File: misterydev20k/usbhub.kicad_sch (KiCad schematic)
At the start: 21 parts, among them J10 USB_A, J7 USB_A, J8 USB_A, J9 USB_A, U7 CH334U, Y3 12MHz

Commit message: More updates in dev20k
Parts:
- removed JP2: CLK, Jumper:SolderJumper-3_P1.3mm_Bridged12_RoundedPad1.0x1.5mm, symbol Jumper:SolderJumper_3_Bridged12
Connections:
- net at U7.3 (XI): now also Y3.1
- net VDD33: no longer names the net of C30.2, C31.2, C32.2, D11.2 (A), U7.13 (VDD33), U7.21 (VDD33)
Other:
- note removed: "2-3 to share OSC with RP2040"
- moved on the sheet: C28, C29, C30, C31, C32, D10, D11, D7, D8, D9, F2, J10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

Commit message: Update board
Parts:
- removed J10, J7, J8, J9: USB_A, Connector_USB:USB_A_Molex_67643_Horizontal, symbol Connector:USB_A
- added J13, J7: USB_A_Stacked, Connector_USB:USB_A_Wuerth_61400826021_Horizontal_Stacked, symbol misteryshield20kpico:USB_A_Stacked
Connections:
- net GND: now also J13.4 (GND1), J13.8 (GND2), J13.9 (Shield), J7.4 (GND1), J7.8 (GND2), J7.9 (Shield)
- net USB1_D+: now also J13.3 (D1+)
- net USB1_D-: now also J13.2 (D1-)
- net USB2_D+: now also J13.7 (D2+)
- net USB2_D-: now also J13.6 (D2-)
- net USB3_D+: now also J7.3 (D1+)
- net USB3_D-: now also J7.2 (D1-)
- net USB4_D+: now also J7.7 (D2+)
- net USB4_D-: now also J7.6 (D2-)
- net at F2.1: now also J13.1 (VBUS1), J13.5 (VBUS2), J7.1 (VBUS1), J7.5 (VBUS2)
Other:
- moved on the sheet: F2

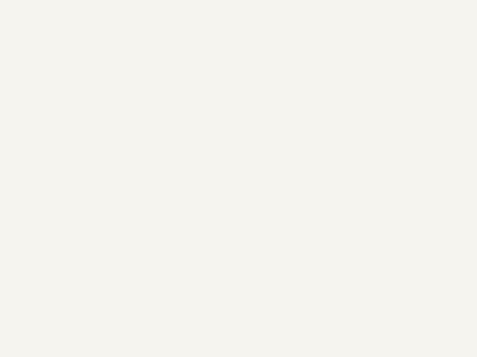
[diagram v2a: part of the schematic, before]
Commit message: Fix dev20k schematic
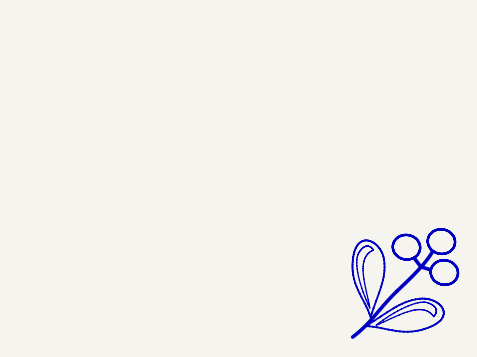
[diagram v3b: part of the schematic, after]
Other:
- company: Stefan Voss -> Stefan Voss, Till Harbaum
- title: MiSTeryShield20KRPiPico -> MiSTeryDev20k - USB Hub

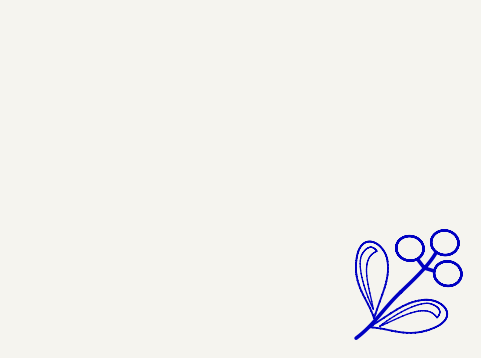
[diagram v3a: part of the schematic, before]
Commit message: Update pin table
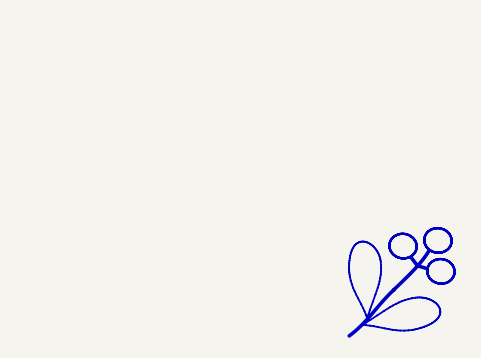
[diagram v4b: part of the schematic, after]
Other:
- title: MiSTeryDev20k - USB Hub -> MiSTle - MiSTeryDev20k

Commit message: Update dev20k pinout
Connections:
- net USB-D+ renamed USB_D+
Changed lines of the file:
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@@
 		)
 	)
-	(hierarchical_label "USB-D+"
+	(hierarchical_label "USB_D+"
 		(shape bidirectional)
 		(at 73.66 66.04 180)

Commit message: Dev20k LCSC part mapping
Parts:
- C28: LCSC C1525 -> (none); LCSC Part # (none) -> C1525; checked (none) -> once
- C29, C32: Comment 0805 -> Samsung 25V X5R; LCSC Part # C28323 -> C52923; checked (none) -> once
- C30: Comment 0805 -> (none); LCSC C1525 -> (none); LCSC Part # (none) -> C1525; checked (none) -> once
- C31: Comment 0805 -> Samsung 6.3V X5R; LCSC Part # C15850 -> C15525; checked (none) -> once
- D10, D11, D7, D8, D9: LCSC C2297 -> (none); LCSC Part # (none) -> C2297; checked (none) -> once
- F2: LCSC C70076 -> (none); LCSC Part # (none) -> C70076; checked (none) -> once
- J13, J7, U7, Y3: checked (none) -> once
- R33, R34: LCSC Part # (none) -> C25091; checked (none) -> once
- R35: LCSC Part # (none) -> C25117; checked (none) -> once
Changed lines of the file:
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@@
 			)
 		)
-		(property "LCSC" "C2297"
+		(property "checked" "once"
+			(at 90.17 113.03 0)
+			(effects
+				(font
+					(size 1.27 1.27)
+				)
+				(hide yes)
+			)
+		)
+		(property "LCSC Part #" "C2297"
 			(at 90.17 113.03 0)
 			(effects
@@
 			)
 		)
-		(property "LCSC" ""
-			(at 81.28 115.57 0)
+		(property "checked" "once"
+			(at 81.28 115.57 90)
+			(effects
+				(font
+					(size 1.27 1.27)
+				)
+				(hide yes)
+			)
+		)
+		(property "LCSC Part #" "C25091"
+			(at 81.28 115.57 90)
 			(effects
 				(font
@@
 			)
 		)
-		(property "LCSC" "C70076"
-			(at 196.85 55.88 0)
+		(property "checked" "once"
+			(at 196.85 55.88 90)
+			(effects
+				(font
+					(size 1.27 1.27)
+				)
+				(hide yes)
+			)
+		)
+		(property "LCSC Part #" "C70076"
+			(at 196.85 55.88 90)
 			(effects
 				(font
@@
 			)
 		)
-		(property "LCSC" "C2297"
+		(property "checked" "once"
+			(at 90.17 118.11 0)
+			(effects
+				(font
+					(size 1.27 1.27)
+				)
+				(hide yes)
+			)
+		)
+		(property "LCSC Part #" "C2297"
 			(at 90.17 118.11 0)
 			(effects
@@
 			)
 		)
-		(property "LCSC" ""
-			(at 81.28 102.87 0)
+		(property "checked" "once"
+			(at 81.28 102.87 90)
+			(effects
+				(font
+					(size 1.27 1.27)
+				)
+				(hide yes)
+			)
+		)
+		(property "LCSC Part #" "C25091"
+			(at 81.28 102.87 90)
 			(effects
 				(font
@@
 			)
 		)
-		(property "LCSC" "C2297"
+		(property "checked" "once"
+			(at 90.17 105.41 0)
+			(effects
+				(font
+					(size 1.27 1.27)
+				)
+				(hide yes)
+			)
+		)
+		(property "LCSC Part #" "C2297"
 			(at 90.17 105.41 0)
 			(effects
@@
 			)
 		)
-		(property "LCSC Part #" ""
+		(property "LCSC Part #" "C1525"
 			(at 97.79 82.55 0)
 			(effects
@@
 			)
 		)
-		(property "Comment" "0805"
+		(property "Comment" ""
 			(at 97.79 82.55 0)
 			(effects
@@
 			)
 		)
-		(property "LCSC" "C1525"
+		(property "checked" "once"
 			(at 97.79 82.55 0)
 			(effects
@@
 			)
 		)
-		(property "LCSC Part #" "C28323"
+		(property "LCSC Part #" "C52923"
 			(at 90.17 82.55 0)
 			(effects
@@
 			)
 		)
-		(property "Comment" "0805"
+		(property "Comment" "Samsung 25V X5R"
+			(at 90.17 82.55 0)
+			(effects
+				(font
+					(size 1.27 1.27)
+				)
+				(hide yes)
+			)
+		)
+		(property "checked" "once"
 			(at 90.17 82.55 0)
 			(effects
@@
 			)
 		)
+		(property "checked" "once"
+			(at 140.97 80.01 0)
+			(effects
+				(font
+					(size 1.27 1.27)
+				)
+				(hide yes)
+			)
+		)
 		(pin "1"
 		)
@@
 			)
 		)
-		(property "LCSC" "C2297"
+		(property "checked" "once"
+			(at 90.17 100.33 0)
+			(effects
+				(font
+					(size 1.27 1.27)
+				)
+				(hide yes)
+			)
+		)
+		(property "LCSC Part #" "C2297"
 			(at 90.17 100.33 0)
 			(effects
@@
 			)
 		)
-		(property "LCSC Part #" "C15850"
+		(property "LCSC Part #" "C15525"
 			(at 105.41 82.55 0)
 			(effects
@@
 			)
 		)
-		(property "Comment" "0805"
+		(property "Comment" "Samsung 6.3V X5R"
+			(at 105.41 82.55 0)
+			(effects
+				(font
+					(size 1.27 1.27)
+				)
+				(hide yes)
+			)
+		)
+		(property "checked" "once"
 			(at 105.41 82.55 0)
 			(effects
@@
 			)
 		)
+		(property "checked" "once"
+			(at 231.14 107.95 0)
+			(effects
+				(font
+					(size 1.27 1.27)
+				)
+				(hide yes)
+			)
+		)
 		(pin "8"
 		)
@@
 			)
 		)
-		(property "LCSC" "C1525"
+		(property "LCSC Part #" "C1525"
 			(at 82.55 82.55 0)
 			(effects
@@
 			)
 		)
-		(property "LCSC Part #" ""
+		(property "checked" "once"
 			(at 82.55 82.55 0)
 			(effects
@@
 			)
 		)
-		(property "LCSC Part #" "C28323"
+		(property "LCSC Part #" "C52923"
 			(at 163.83 54.61 0)
 			(effects
@@
 			)
 		)
-		(property "Comment" "0805"
+		(property "Comment" "Samsung 25V X5R"
 			(at 163.83 54.61 0)
+			(effects
+				(font
+					(size 1.27 1.27)
+				)
+				(hide yes)
+			)
+		)
+		(property "checked" "once"
+			(at 163.83 54.61 90)
 			(effects
 				(font
@@
 			)
 		)
+		(property "checked" "once"
+			(at 231.14 66.04 0)
+			(effects
+				(font
+					(size 1.27 1.27)
+				)
+				(hide yes)
+			)
+		)
 		(pin "8"
 		)
@@
 		)
 		(property "Comment" "SMD 3225 4-Pin"
+			(at 168.91 101.6 0)
+			(effects
+				(font
+					(size 1.27 1.27)
+				)
+				(hide yes)
+			)
+		)
+		(property "checked" "once"
 			(at 168.91 101.6 0)
 			(effects
@@
 			)
 		)
-		(property "LCSC" ""
-			(at 106.68 127 0)
+		(property "checked" "once"
+			(at 106.68 127 90)
+			(effects
+				(font
+					(size 1.27 1.27)
+				)
+				(hide yes)
+			)
+		)
+		(property "LCSC Part #" "C25117"
+			(at 106.68 127 90)
 			(effects
 				(font
@@
 			)
 		)
-		(property "LCSC" "C2297"
-			(at 113.03 106.68 0)
-			(effects
-				(font
+		(property "checked" "once"
+			(at 113.03 106.68 90)
+			(effects
+				(font
+					(size 1.27 1.27)
+				)
+				(hide yes)
+			)
+		)
+		(property "LCSC Part #" "C2297"
+			(at 113.03 106.68 90)
+			(effects
+				(font

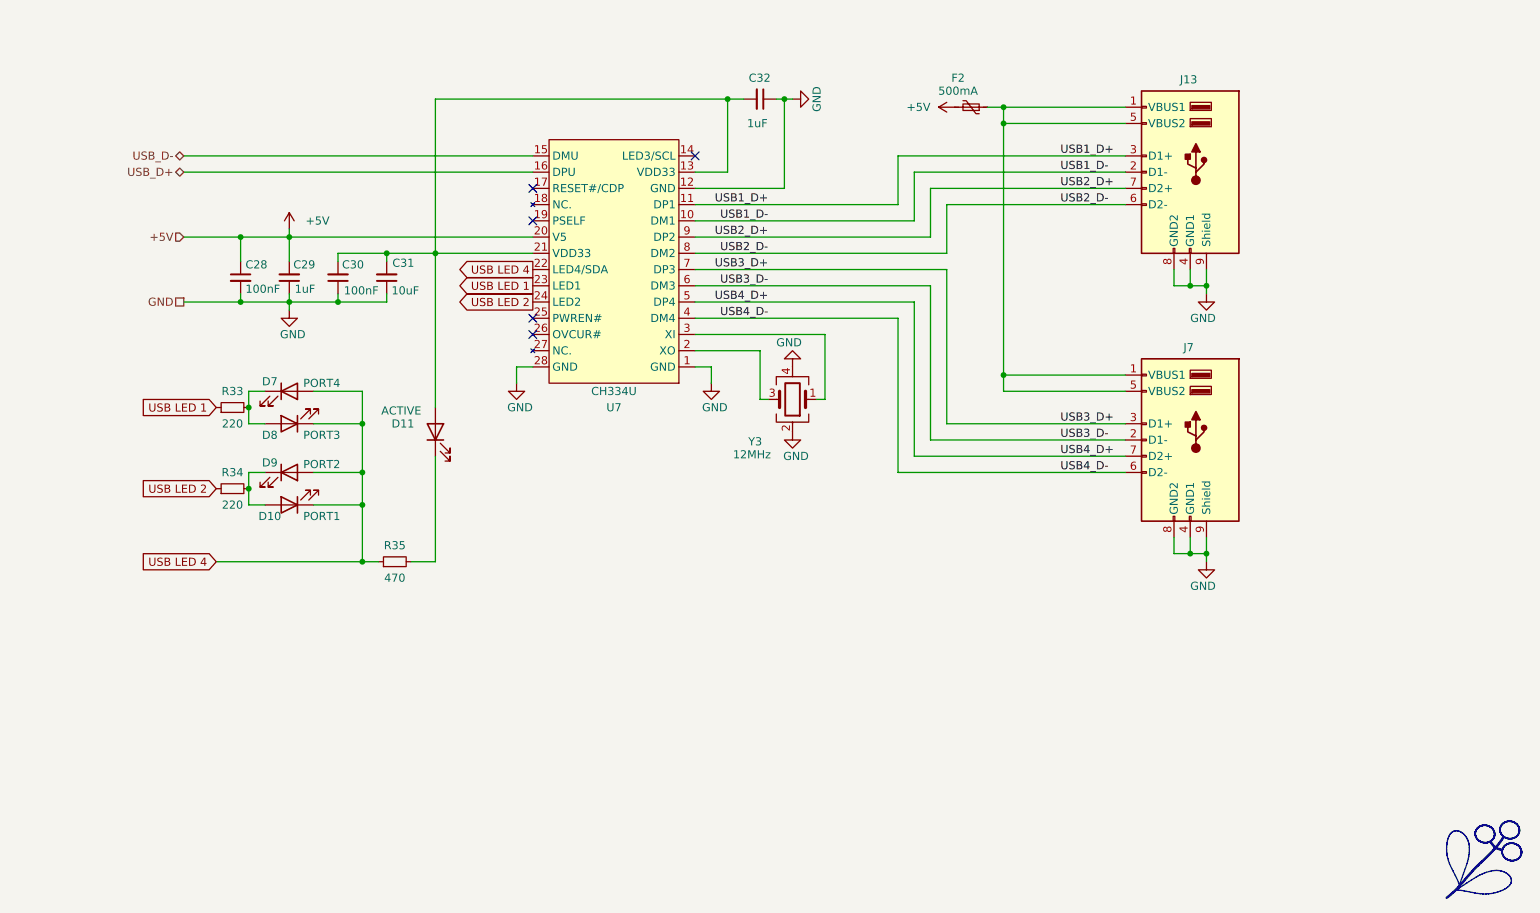
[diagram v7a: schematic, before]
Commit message: Replace ch334u by ch334r due to availablity
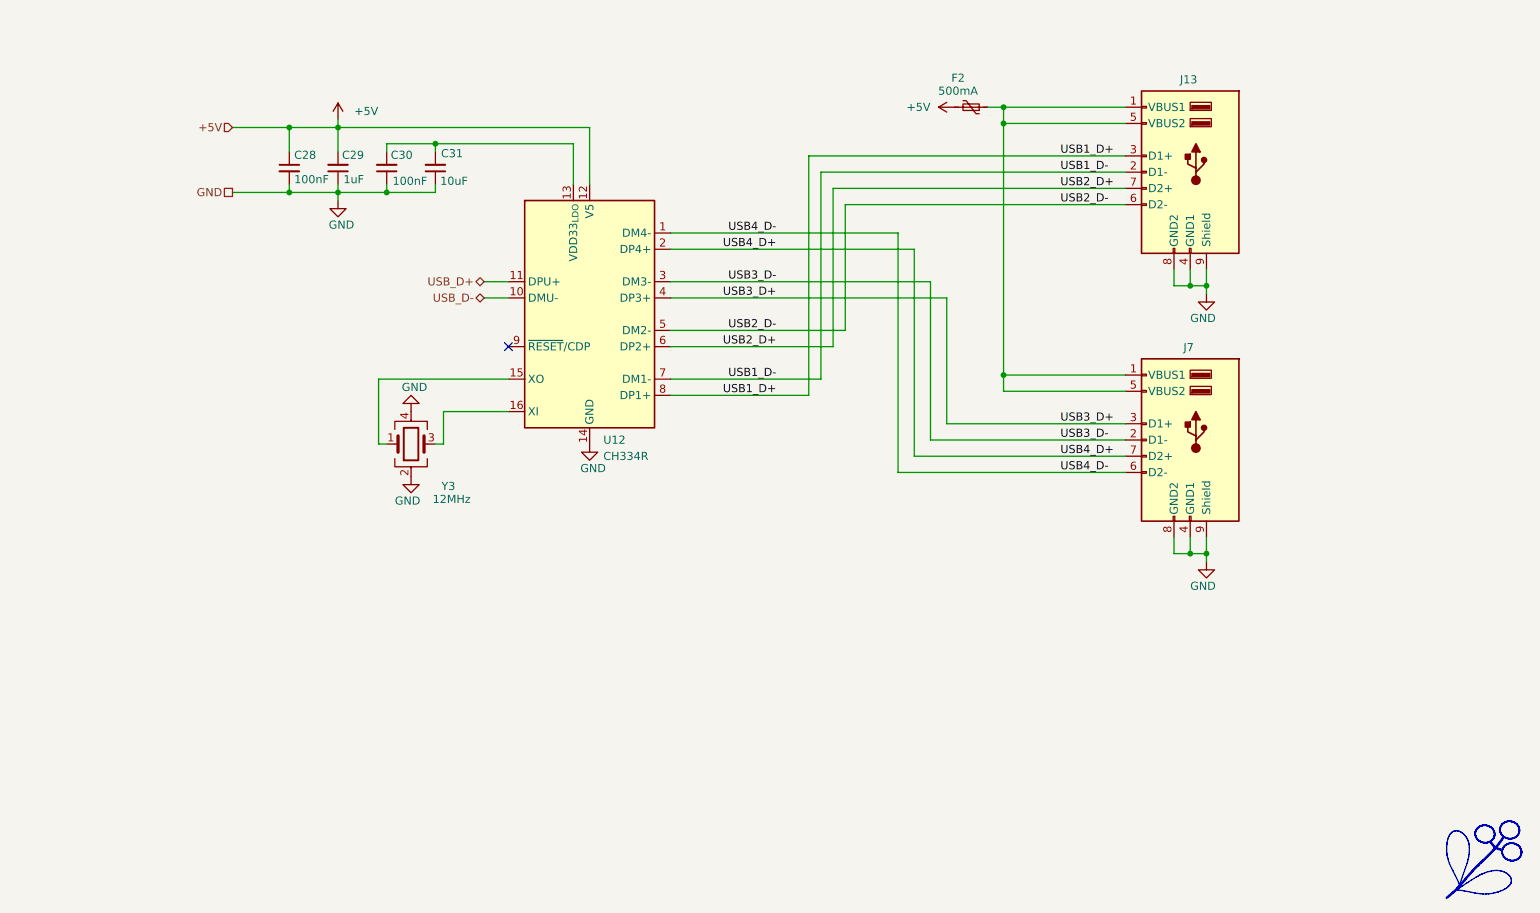
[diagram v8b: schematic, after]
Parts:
- removed C32: 1uF, Capacitor_SMD:C_0402_1005Metric, symbol Device:C_Small
- removed D10: PORT1, LED_SMD:LED_0805_2012Metric, symbol Device:LED
- removed D11: ACTIVE, LED_SMD:LED_0805_2012Metric, symbol Device:LED
- removed D7: PORT4, LED_SMD:LED_0805_2012Metric, symbol Device:LED
- removed D8: PORT3, LED_SMD:LED_0805_2012Metric, symbol Device:LED
- removed D9: PORT2, LED_SMD:LED_0805_2012Metric, symbol Device:LED
- removed R33, R34: 220, Resistor_SMD:R_0402_1005Metric, symbol Device:R_Small
- removed R35: 470, Resistor_SMD:R_0402_1005Metric, symbol Device:R_Small
- removed U7: CH334U, Package_SO:SSOP-28_3.9x9.9mm_P0.635mm, symbol wch_mcu_peripheral:CH334U
- added U12: CH334R, Package_SO:QSOP-16_3.9x4.9mm_P0.635mm, symbol Interface_USB:CH334R
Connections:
- net +5V: now also U12.12 (V5)
- net GND: now also U12.14 (GND)
- net USB1_D+: now also U12.8 (DP1+)
- net USB1_D-: now also U12.7 (DM1-)
- net USB2_D+: now also U12.6 (DP2+)
- net USB2_D-: now also U12.5 (DM2-)
- net USB3_D+: now also U12.4 (DP3+)
- net USB3_D-: now also U12.3 (DM3-)
- net USB4_D+: now also U12.2 (DP4+)
- net USB4_D-: now also U12.1 (DM4-)
- net USB_D+: now also U12.11 (DPU+)
- net USB_D-: now also U12.10 (DMU-)
- net at C30.2, C31.2: now also U12.13 (VDD33_{LDO})
- net at Y3.3: now also U12.16 (XI)
- net at Y3.1: now also U12.15 (XO)
- no-connect marks 5 -> 1
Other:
- moved on the sheet: C28, C29, C30, C31, Y3
